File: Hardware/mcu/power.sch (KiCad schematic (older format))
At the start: 13 parts, among them J601 USB-A, P601 MainPwr, U601 LM317, U602 LM1117-3.3, U603 LM317

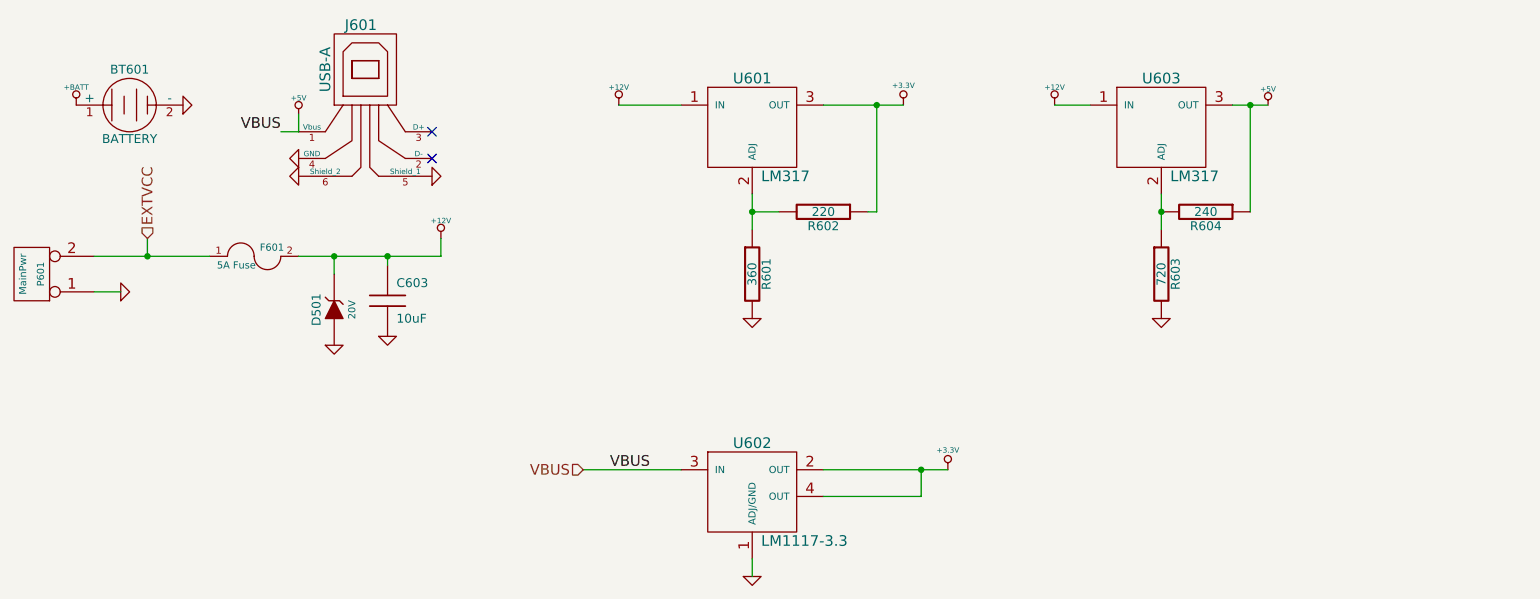
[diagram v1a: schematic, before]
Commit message: changes to mcu, new format and using a display adapter board
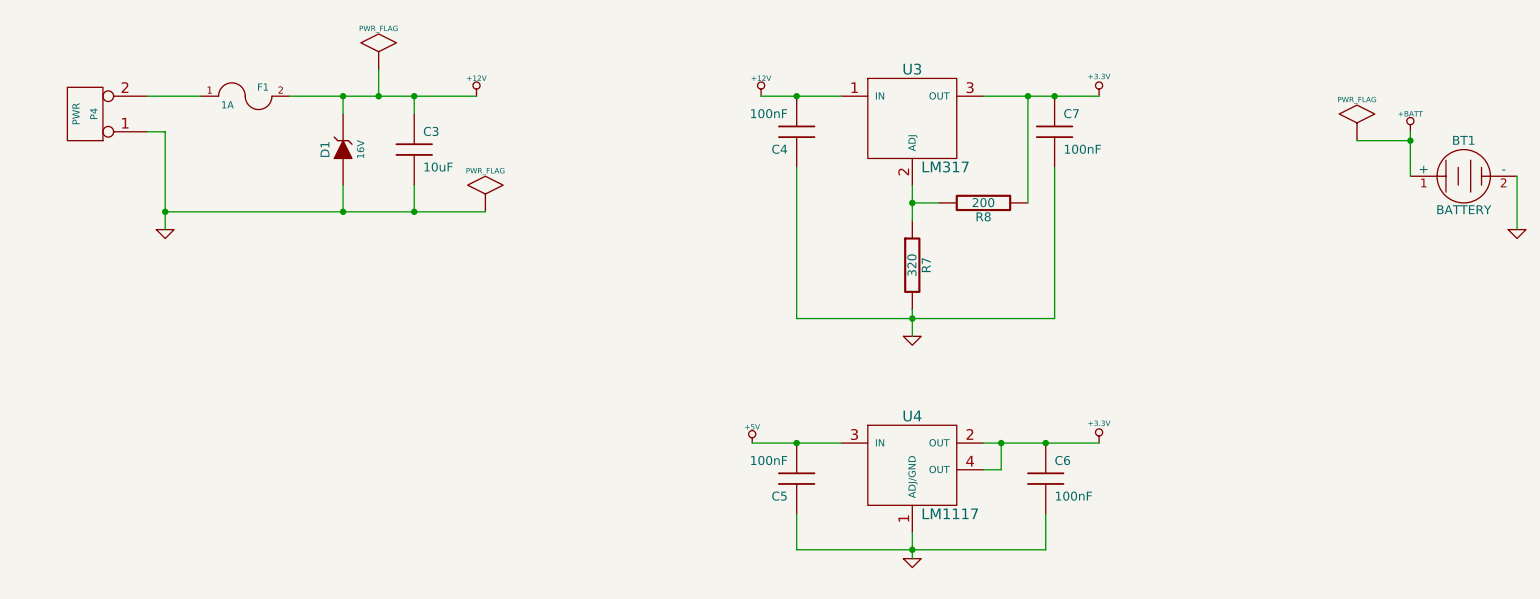
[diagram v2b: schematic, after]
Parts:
- removed BT601: BATTERY, symbol BATTERY
- removed C603: 10uF, symbol C
- removed D501: 20V, symbol ZENER
- removed F601: 5A Fuse, littelfuse, symbol FUSE
- removed J601: USB-A, symbol USB
- removed P601: MainPwr, symbol CONN_2
- removed R601: 360, symbol R
- removed R602: 220, symbol R
- removed R603: 720, symbol R
- removed R604: 240, symbol R
- removed U601, U603: LM317, symbol LM317
- removed U602: LM1117-3.3, symbol LM1117
- added BT1: BATTERY, symbol BATTERY
- added C3: 10uF, symbol C
- added C4, C5, C6, C7: 100nF, symbol C
- added D1: 16V, symbol ZENER
- added F1: 1A, symbol FUSE
- added P4: PWR, symbol CONN_2
- added R7: 320, symbol R
- added R8: 200, symbol R
- added U3: LM317, symbol LM317
- added U4: LM1117, symbol LM1117
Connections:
- net +12V: now also C3.1, C4.2, D1.2 (K), F1.2, U3.1 (IN)
- net +3.3V: now also C6.1, C7.1, R8.1, U3.3 (OUT), U4.2 (OUT), U4.4 (OUT)
- net +5V: now also C5.2, U4.3 (IN)
- net +BATT: now also BT1.1 (+)
- net GND: now also BT1.2 (-), C3.2, C4.1, C5.1, C6.2, C7.2, D1.1 (A), P4.1 (P1), R7.2, U4.1 (ADJ/GND)
- new net: F1.1, P4.2 (PM)
- new net: R7.1, R8.2, U3.2 (ADJ)
- no-connect marks 2 -> 0
